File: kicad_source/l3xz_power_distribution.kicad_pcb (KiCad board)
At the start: 2 copper layers, 73 x 24 mm, 16 parts, among them J1 PowerPole_ver, J2 PowerPole_ver, J3 PowerPole_ver, J4 PowerPole_ver, J5 PowerPole_ver, J6 PowerPole_ver, J7 PowerPole_ver, J8 PowerPole_ver

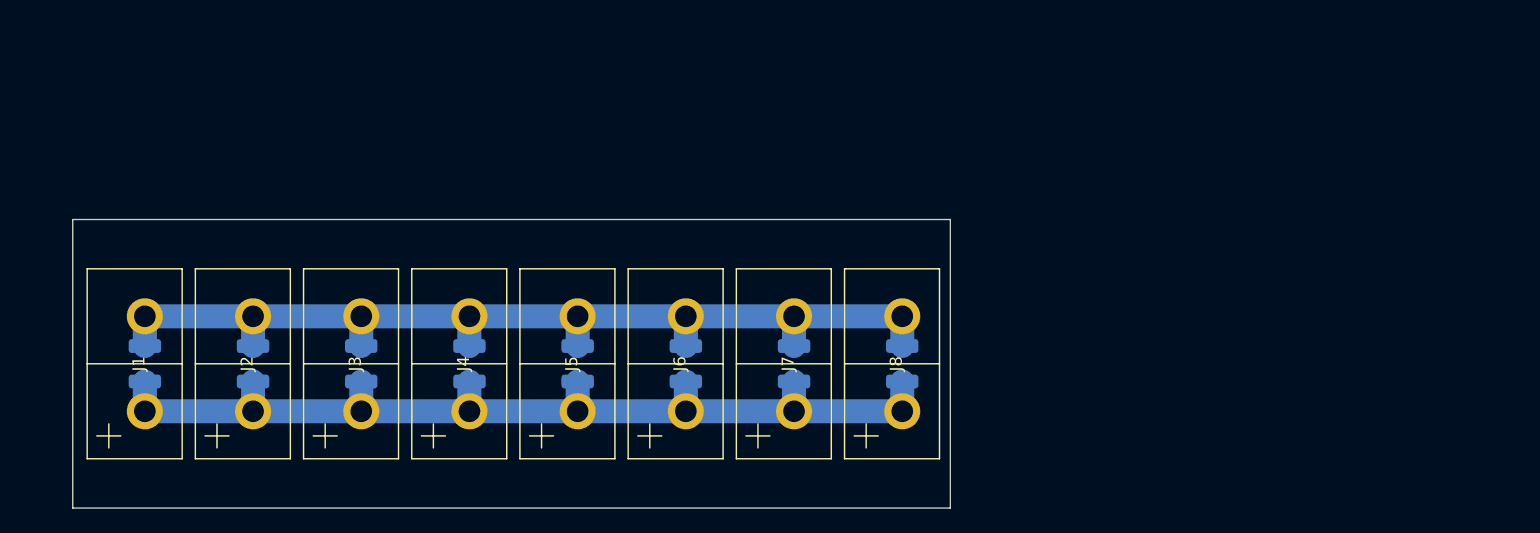
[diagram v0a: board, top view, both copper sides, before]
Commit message: added 4 more power poles
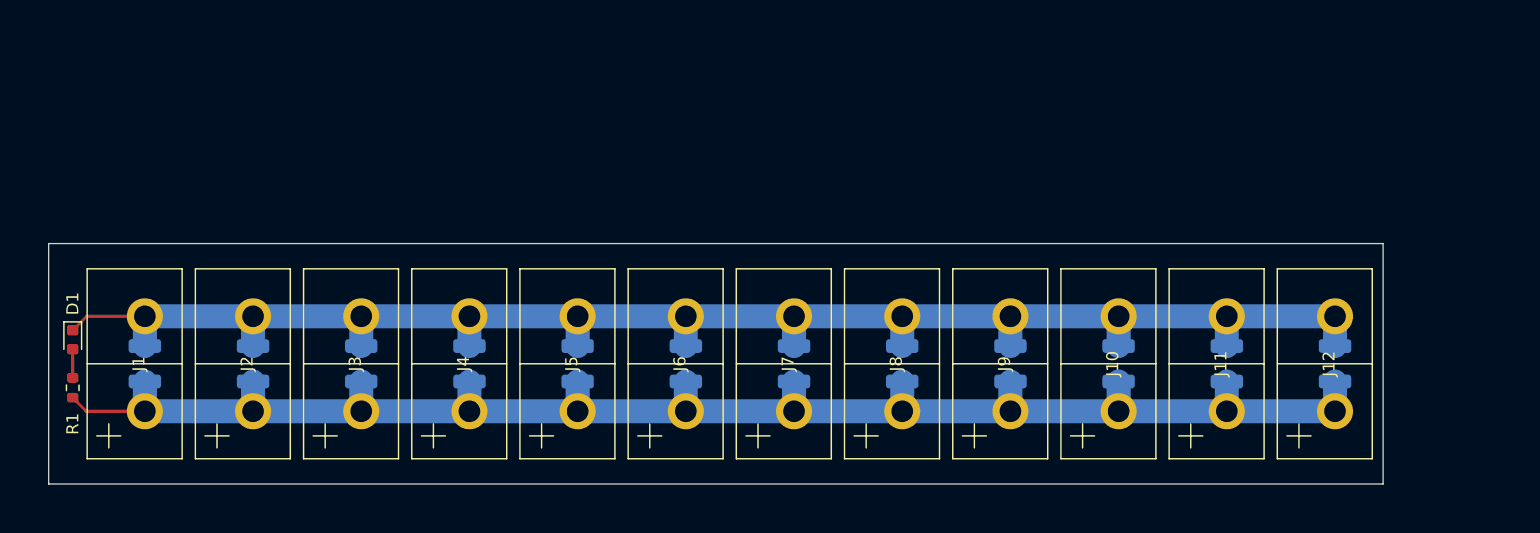
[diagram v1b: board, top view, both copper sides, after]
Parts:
- added C10: 10 uF 25 V, Capacitor_SMD:C_1210_3225Metric, B.Cu at (181.0, 100.0)
- added C11: 10 uF 25 V, Capacitor_SMD:C_1210_3225Metric, B.Cu at (190.0, 100.0)
- added C12: 10 uF 25 V, Capacitor_SMD:C_1210_3225Metric, B.Cu at (199.0, 100.0)
- added C9: 10 uF 25 V, Capacitor_SMD:C_1210_3225Metric, B.Cu at (172.0, 100.0)
- added D1: LED_Small, LED_SMD:LED_0603_1608Metric, F.Cu at (94.0, 98.0)
- added J10: PowerPole_ver, generationmake:POWERPOLE_2, F.Cu at (181.0, 100.0)
- added J11: PowerPole_ver, generationmake:POWERPOLE_2, F.Cu at (190.0, 100.0)
- added J12: PowerPole_ver, generationmake:POWERPOLE_2, F.Cu at (199.0, 100.0)
- added J9: PowerPole_ver, generationmake:POWERPOLE_2, F.Cu at (172.0, 100.0)
- added R1: 10k, Resistor_SMD:R_0603_1608Metric, F.Cu at (94.0, 102.0)
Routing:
- net GND: track 82.8 -> 135.2 mm
- net +BATT: track 82.8 -> 135.2 mm
- net Net-(D1-Pad2): track 0.00 -> 2.39 mm
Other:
- board size 73 x 24 mm -> 111 x 20 mm

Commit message: added some labels
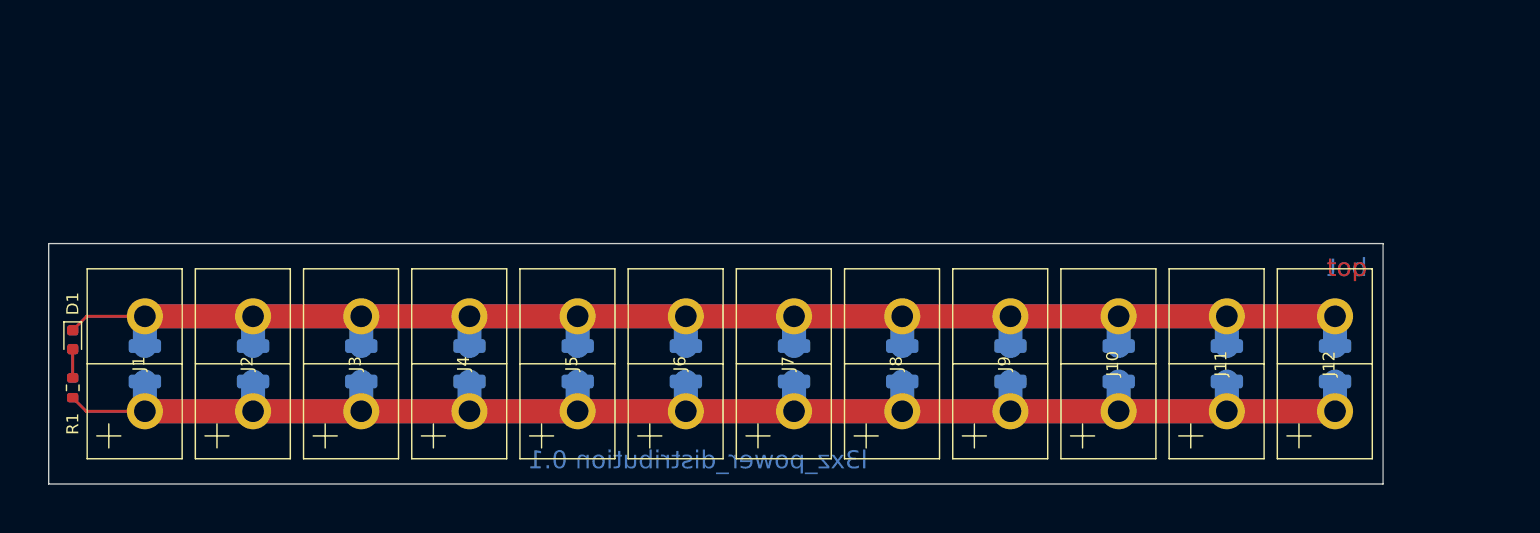
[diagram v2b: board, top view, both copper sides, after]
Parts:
- added L1: Label, generationmake:generationmake_logo, B.Cu at (148.0, 97.4)
- added L2: Label, generationmake:l3xz_small_silk, B.Cu at (98.0, 95.0)
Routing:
- net GND: track 135.2 -> 234.2 mm
- net +BATT: track 135.2 -> 234.2 mm
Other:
- board text added: "bot"
- board text added: "l3xz_power_distribution 0.1"
- board text added: "top"

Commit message: moved to horizontal power poles
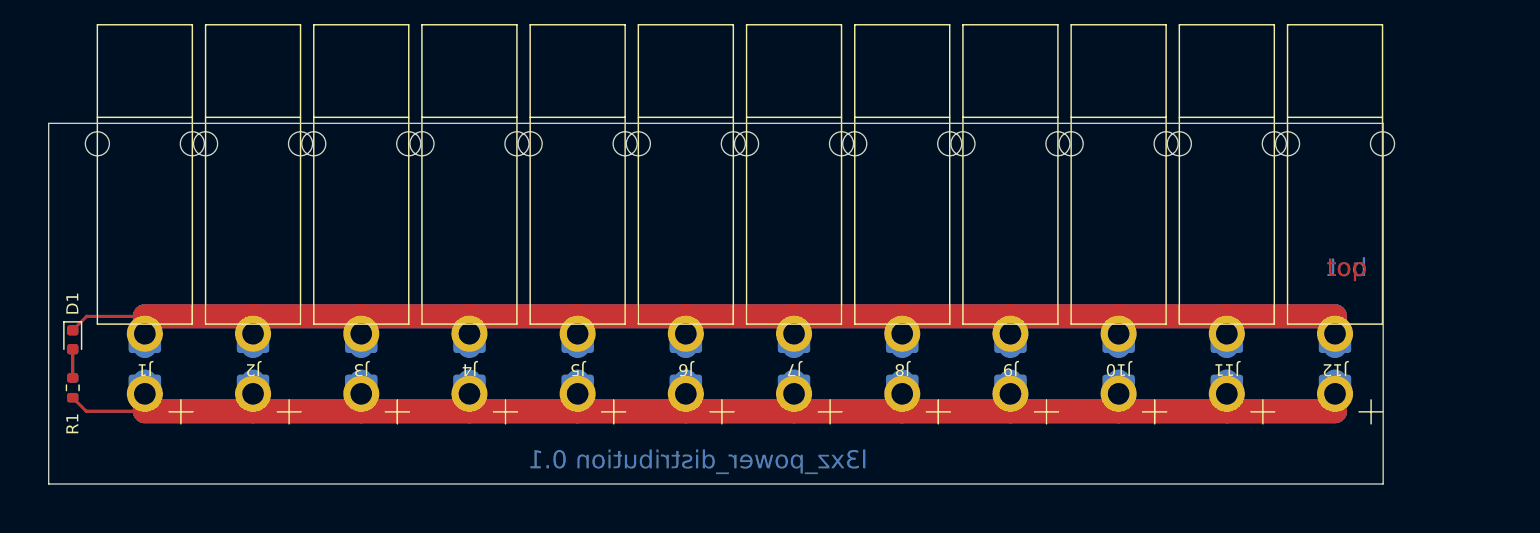
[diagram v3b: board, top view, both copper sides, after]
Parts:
- J1, J10, J11, J12, J2, J3, J4, J5, J6, J7, J8, J9: footprint generationmake:POWERPOLE_2 -> generationmake:POWERPOLE_hor90_2
- turned J1 to 180 degrees
- turned J10 to 180 degrees
- turned J11 to 180 degrees
- turned J12 to 180 degrees
- turned J2 to 180 degrees
- turned J3 to 180 degrees
- turned J4 to 180 degrees
- turned J5 to 180 degrees
- turned J6 to 180 degrees
- turned J7 to 180 degrees
- turned J8 to 180 degrees
- turned J9 to 180 degrees
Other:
- board size 111 x 20 mm -> 111 x 30 mm

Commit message: added mounting holes
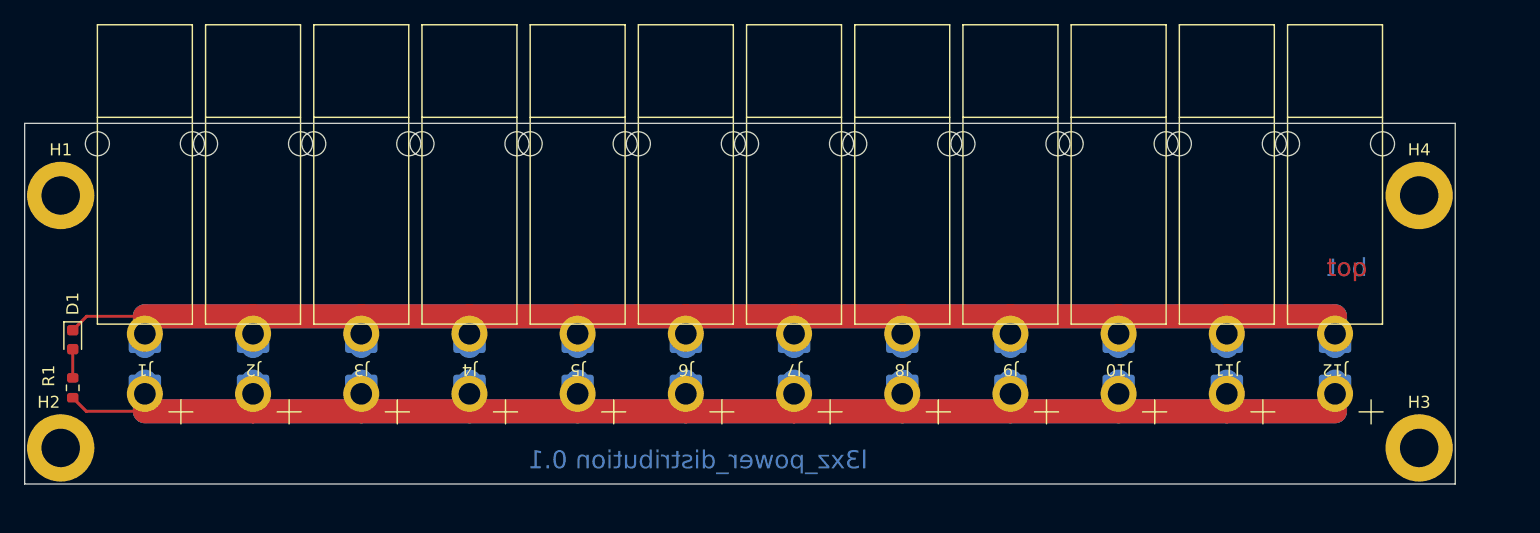
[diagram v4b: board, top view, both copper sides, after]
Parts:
- added H1: MountingHole_Pad, MountingHole:MountingHole_3.2mm_M3_DIN965_Pad, F.Cu at (93.0, 86.0)
- added H2: MountingHole_Pad, MountingHole:MountingHole_3.2mm_M3_DIN965_Pad, F.Cu at (93.0, 107.0)
- added H3: MountingHole_Pad, MountingHole:MountingHole_3.2mm_M3_DIN965_Pad, F.Cu at (206.0, 107.0)
- added H4: MountingHole_Pad, MountingHole:MountingHole_3.2mm_M3_DIN965_Pad, F.Cu at (206.0, 86.0)
- moved L2 5.00 mm to (101.0, 91.0)
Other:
- board size 111 x 30 mm -> 119 x 30 mm
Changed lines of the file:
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@@
   (net 2 "GND")
   (net 3 "Net-(D1-Pad2)")
+  (net 4 "unconnected-(H1-Pad1)")
+  (net 5 "unconnected-(H2-Pad1)")
+  (net 6 "unconnected-(H3-Pad1)")
+  (net 7 "unconnected-(H4-Pad1)")
+  (footprint "MountingHole:MountingHole_3.2mm_M3_DIN965_Pad" (layer "F.Cu")
+    (at 93 86)
+    (descr "Mounting Hole 3.2mm, M3, DIN965")
+    (tags "mounting hole 3.2mm m3 din965")
+    (property "Sheetfile" "l3xz_power_distribution.kicad_sch")
+    (property "Sheetname" "")
+    (attr exclude_from_pos_files)
+    (fp_text reference "H1" (at 0 -3.8) (layer "F.SilkS")
+      (effects (font (size 1 1) (thickness 0.15)))
+    )
+    (fp_text value "MountingHole_Pad" (at 0 3.8) (layer "F.Fab")
+      (effects (font (size 1 1) (thickness 0.15)))
+    )
+    (fp_text user "${REFERENCE}" (at 0 0) (layer "F.Fab")
+      (effects (font (size 1 1) (thickness 0.15)))
+    )
+    (fp_circle (center 0 0) (end 2.8 0) (layer "Cmts.User") (width 0.15) (fill none))
+    (fp_circle (center 0 0) (end 3.05 0) (layer "F.CrtYd") (width 0.05) (fill none))
+    (pad "1" thru_hole circle (at 0 0) (size 5.6 5.6) (drill 3.2) (layers *.Cu *.Mask)
+      (net 4 "unconnected-(H1-Pad1)") (pinfunction "1") (pintype "input+no_connect"))
+  )
+  (footprint "MountingHole:MountingHole_3.2mm_M3_DIN965_Pad" (layer "F.Cu")
+    (at 93 107)
+    (descr "Mounting Hole 3.2mm, M3, DIN965")
+    (tags "mounting hole 3.2mm m3 din965")
+    (property "Sheetfile" "l3xz_power_distribution.kicad_sch")
+    (property "Sheetname" "")
+    (attr exclude_from_pos_files)
+    (fp_text reference "H2" (at -1 -3.8) (layer "F.SilkS")
+      (effects (font (size 1 1) (thickness 0.15)))
+    )
+    (fp_text value "MountingHole_Pad" (at 0 3.8) (layer "F.Fab")
+      (effects (font (size 1 1) (thickness 0.15)))
+    )
+    (fp_text user "${REFERENCE}" (at 0 0) (layer "F.Fab")
+      (effects (font (size 1 1) (thickness 0.15)))
+    )
+    (fp_circle (center 0 0) (end 2.8 0) (layer "Cmts.User") (width 0.15) (fill none))
+    (fp_circle (center 0 0) (end 3.05 0) (layer "F.CrtYd") (width 0.05) (fill none))
+    (pad "1" thru_hole circle (at 0 0) (size 5.6 5.6) (drill 3.2) (layers *.Cu *.Mask)
+      (net 5 "unconnected-(H2-Pad1)") (pinfunction "1") (pintype "input+no_connect"))
+  )
   (footprint "generationmake:POWERPOLE_hor90_2" (layer "F.Cu")
     (at 181 100 180)
@@
     )
   )
+  (footprint "MountingHole:MountingHole_3.2mm_M3_DIN965_Pad" (layer "F.Cu")
+    (at 206 107)
+    (descr "Mounting Hole 3.2mm, M3, DIN965")
+    (tags "mounting hole 3.2mm m3 din965")
+    (property "Sheetfile" "l3xz_power_distribution.kicad_sch")
+    (property "Sheetname" "")
+    (attr exclude_from_pos_files)
+    (fp_text reference "H3" (at 0 -3.8) (layer "F.SilkS")
+      (effects (font (size 1 1) (thickness 0.15)))
+    )
+    (fp_text value "MountingHole_Pad" (at 0 3.8) (layer "F.Fab")
+      (effects (font (size 1 1) (thickness 0.15)))
+    )
+    (fp_text user "${REFERENCE}" (at 0 0) (layer "F.Fab")
+      (effects (font (size 1 1) (thickness 0.15)))
+    )
+    (fp_circle (center 0 0) (end 2.8 0) (layer "Cmts.User") (width 0.15) (fill none))
+    (fp_circle (center 0 0) (end 3.05 0) (layer "F.CrtYd") (width 0.05) (fill none))
+    (pad "1" thru_hole circle (at 0 0) (size 5.6 5.6) (drill 3.2) (layers *.Cu *.Mask)
+      (net 6 "unconnected-(H3-Pad1)") (pinfunction "1") (pintype "input+no_connect"))
+  )
   (footprint "generationmake:POWERPOLE_hor90_2" (layer "F.Cu")
     (at 127 100 180)
@@
     )
   )
+  (footprint "MountingHole:MountingHole_3.2mm_M3_DIN965_Pad" (layer "F.Cu")
+    (at 206 86)
+    (descr "Mounting Hole 3.2mm, M3, DIN965")
+    (tags "mounting hole 3.2mm m3 din965")
+    (property "Sheetfile" "l3xz_power_distribution.kicad_sch")
+    (property "Sheetname" "")
+    (attr exclude_from_pos_files)
+    (fp_text reference "H4" (at 0 -3.8) (layer "F.SilkS")
+      (effects (font (size 1 1) (thickness 0.15)))
+    )
+    (fp_text value "MountingHole_Pad" (at 0 3.8) (layer "F.Fab")
+      (effects (font (size 1 1) (thickness 0.15)))
+    )
+    (fp_text user "${REFERENCE}" (at 0 0) (layer "F.Fab")
+      (effects (font (size 1 1) (thickness 0.15)))
+    )
+    (fp_circle (center 0 0) (end 2.8 0) (layer "Cmts.User") (width 0.15) (fill none))
+    (fp_circle (center 0 0) (end 3.05 0) (layer "F.CrtYd") (width 0.05) (fill none))
+    (pad "1" thru_hole circle (at 0 0) (size 5.6 5.6) (drill 3.2) (layers *.Cu *.Mask)
+      (net 7 "unconnected-(H4-Pad1)") (pinfunction "1") (pintype "input+no_connect"))
+  )
   (footprint "generationmake:POWERPOLE_hor90_2" (layer "F.Cu")
     (at 199 100 180)
@@
     (property "Sheetname" "")
     (attr smd)
-    (fp_text reference "R1" (at -3 0 90) (layer "F.SilkS")
+    (fp_text reference "R1" (at 1 -2 90) (layer "F.SilkS")
       (effects (font (size 1 1) (thickness 0.15)))
     )
@@
   )
   (footprint "generationmake:l3xz_small_silk" (layer "B.Cu")
-    (at 98 95 -90)
+    (at 101 91 -90)
     (property "Sheetfile" "l3xz_power_distribution.kicad_sch")
     (property "Sheetname" "")
     (attr board_only exclude_from_pos_files)
-    (fp_text reference "L2" (at 0 0 90) (layer "B.SilkS")
+    (fp_text reference "L2" (at 0 0 90) (layer "B.SilkS") hide
       (effects (font (size 1.524 1.524) (thickness 0.3)) (justify mirror))
     )
@@
     )
   )
-  (gr_line (start 92 80) (end 203 80) (layer "Edge.Cuts") (width 0.1))
-  (gr_line (start 203 110) (end 92 110) (layer "Edge.Cuts") (width 0.1))
-  (gr_line (start 92 110) (end 92 80) (layer "Edge.Cuts") (width 0.1))
-  (gr_line (start 203 80) (end 203 110) (layer "Edge.Cuts") (width 0.1))
+  (gr_line (start 90 80) (end 209 80) (layer "Edge.Cuts") (width 0.1))
+  (gr_line (start 209 110) (end 90 110) (layer "Edge.Cuts") (width 0.1))
+  (gr_line (start 90 110) (end 90 80) (layer "Edge.Cuts") (width 0.1))
+  (gr_line (start 209 80) (end 209 110) (layer "Edge.Cuts") (width 0.1))
   (gr_text "top" (at 200 92) (layer "F.Cu")
     (effects (font (size 1.5 1.5) (thickness 0.375)))
@@
   )
   (dimension (type aligned) (layer "Cmts.User")
-    (pts (xy 92 110) (xy 92 80))
+    (pts (xy 90 110) (xy 90 80))
     (height -8)
-    (gr_text "30,0000 mm" (at 82.85 95 90) (layer "Cmts.User")
+    (gr_text "30,0000 mm" (at 80.85 95 90) (layer "Cmts.User")
       (effects (font (size 1 1) (thickness 0.15)))
     )
@@
   )
   (dimension (type aligned) (layer "Cmts.User")
-    (pts (xy 92 110) (xy 203 110))
+    (pts (xy 90 110) (xy 209 110))
     (height 9)
-    (gr_text "111,0000 mm" (at 147.5 117.85) (layer "Cmts.User")
+    (gr_text "119,0000 mm" (at 149.5 117.85) (layer "Cmts.User")
       (effects (font (size 1 1) (thickness 0.15)))
     )

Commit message: added additional mounting hole
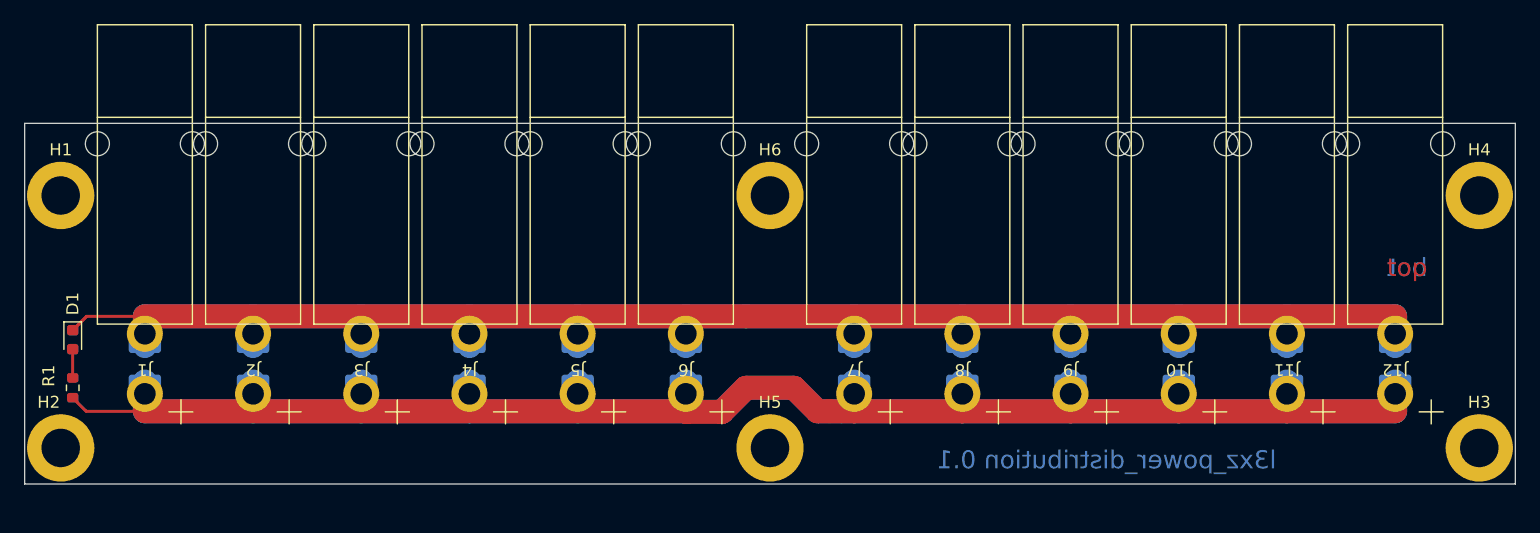
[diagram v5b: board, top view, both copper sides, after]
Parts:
- added H5: MountingHole_Pad, MountingHole:MountingHole_3.2mm_M3_DIN965_Pad, F.Cu at (152.0, 107.0)
- added H6: MountingHole_Pad, MountingHole:MountingHole_3.2mm_M3_DIN965_Pad, F.Cu at (152.0, 86.0)
- moved C10 5.00 mm to (186.0, 100.0)
- moved C11 5.00 mm to (195.0, 100.0)
- moved C12 5.00 mm to (204.0, 100.0)
- moved C7 5.00 mm to (159.0, 100.0)
- moved C8 5.00 mm to (168.0, 100.0)
- moved C9 5.00 mm to (177.0, 100.0)
- moved H3 5.00 mm to (211.0, 107.0)
- moved H4 5.00 mm to (211.0, 86.0)
- moved J10 5.00 mm to (186.0, 100.0)
- moved J11 5.00 mm to (195.0, 100.0)
- moved J12 5.00 mm to (204.0, 100.0)
- moved J7 5.00 mm to (159.0, 100.0)
- moved J8 5.00 mm to (168.0, 100.0)
- moved J9 5.00 mm to (177.0, 100.0)
- moved L1 5.00 mm to (153.0, 97.4)
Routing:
- net +BATT: track 234.2 -> 247.5 mm
- net GND: track 234.2 -> 244.2 mm
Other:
- board size 119 x 30 mm -> 124 x 30 mm
